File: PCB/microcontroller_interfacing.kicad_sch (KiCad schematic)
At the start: 19 parts, among them U3 CH340G, U4 USB_Micro_B, U5 AT24C256C-SSHL-T, X1 12MHz Crystal

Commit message: pcb revive
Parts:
- TP3: value TestPoint -> UsbOn
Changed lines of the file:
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@@
     (in_bom yes) (on_board yes)
     (property "Reference" "TP3" (id 0) (at 139.7 103.505 90))
-    (property "Value" "TestPoint" (id 1) (at 139.065 105.41 90))
+    (property "Value" "UsbOn" (id 1) (at 139.065 105.41 90))
     (property "Footprint" "TestPoint:TestPoint_Pad_D1.0mm" (id 2) (at 149.225 99.695 0)
       (effects (font (size 1.27 1.27)) hide)

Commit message: Add Justin's comments
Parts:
- removed R4: 2.7k, Resistor_SMD:R_0402_1005Metric, symbol Device:R
- removed R5: 4.7k, Resistor_SMD:R_0402_1005Metric, symbol Device:R
- added D?: DIODE, Footprint_EEE3088F:DO-214AC_L4.3-W2.7-LS5.3-RD, symbol Simulation_SPICE:DIODE
- R6: value 82 -> 150; footprint Resistor_SMD:R_0603_1608Metric -> Resistor_SMD:R_0402_1005Metric; JLC Part # C23255 -> C25082; Price 0.0015 -> 0.0007
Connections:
- net +5V: now also D?.2 (K); no longer C7.1, D4.2 (A), U3.4 (V3), U4.1 (VDD)
- net USB On: now also D4.1 (K), R6.1
- new net: C7.1, U3.4 (V3)
- new net USB_Detect: D4.2 (A), D?.1 (A), U4.1 (VDD)
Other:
- moved on the sheet: D4, R6

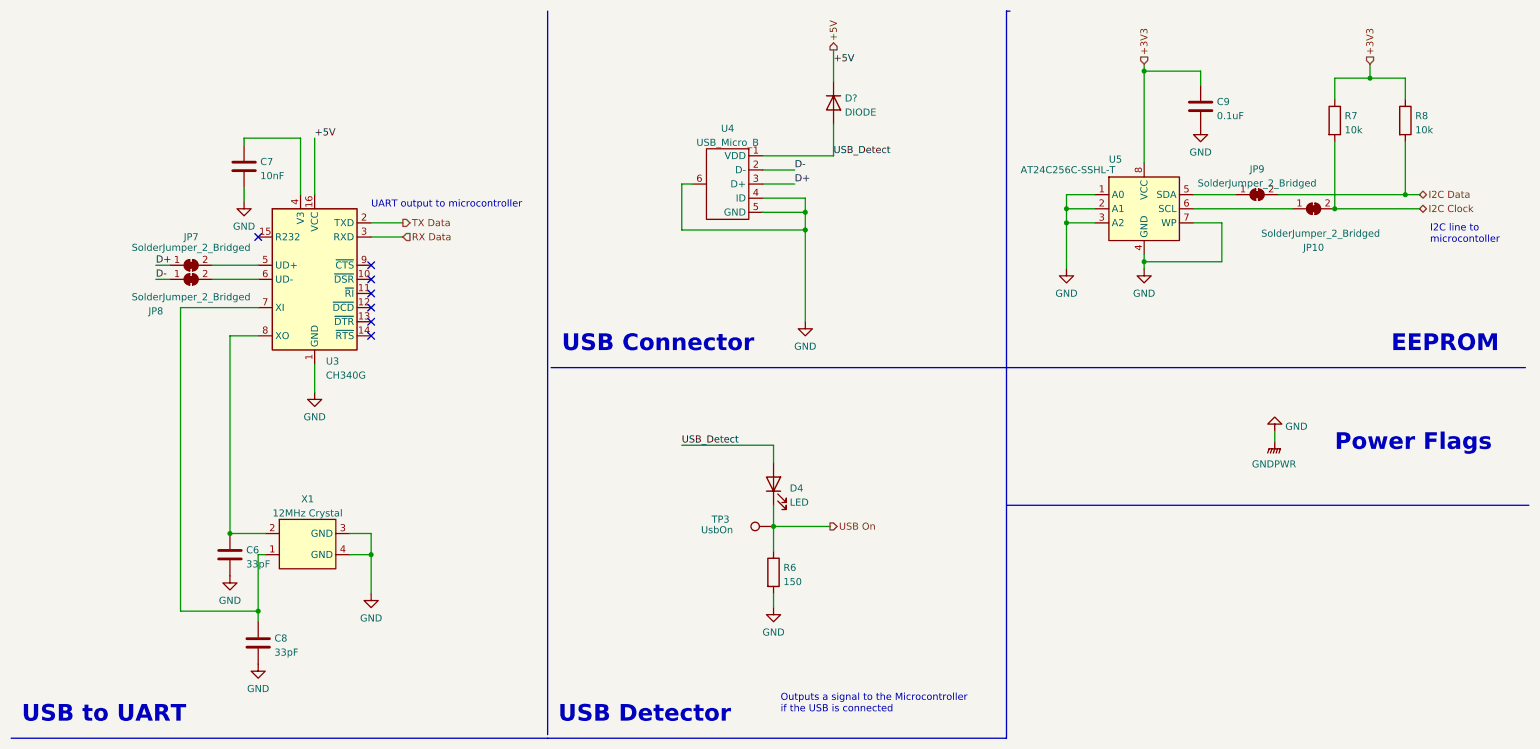
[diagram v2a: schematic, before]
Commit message: Mostly addressed issues with Sensing subsystem
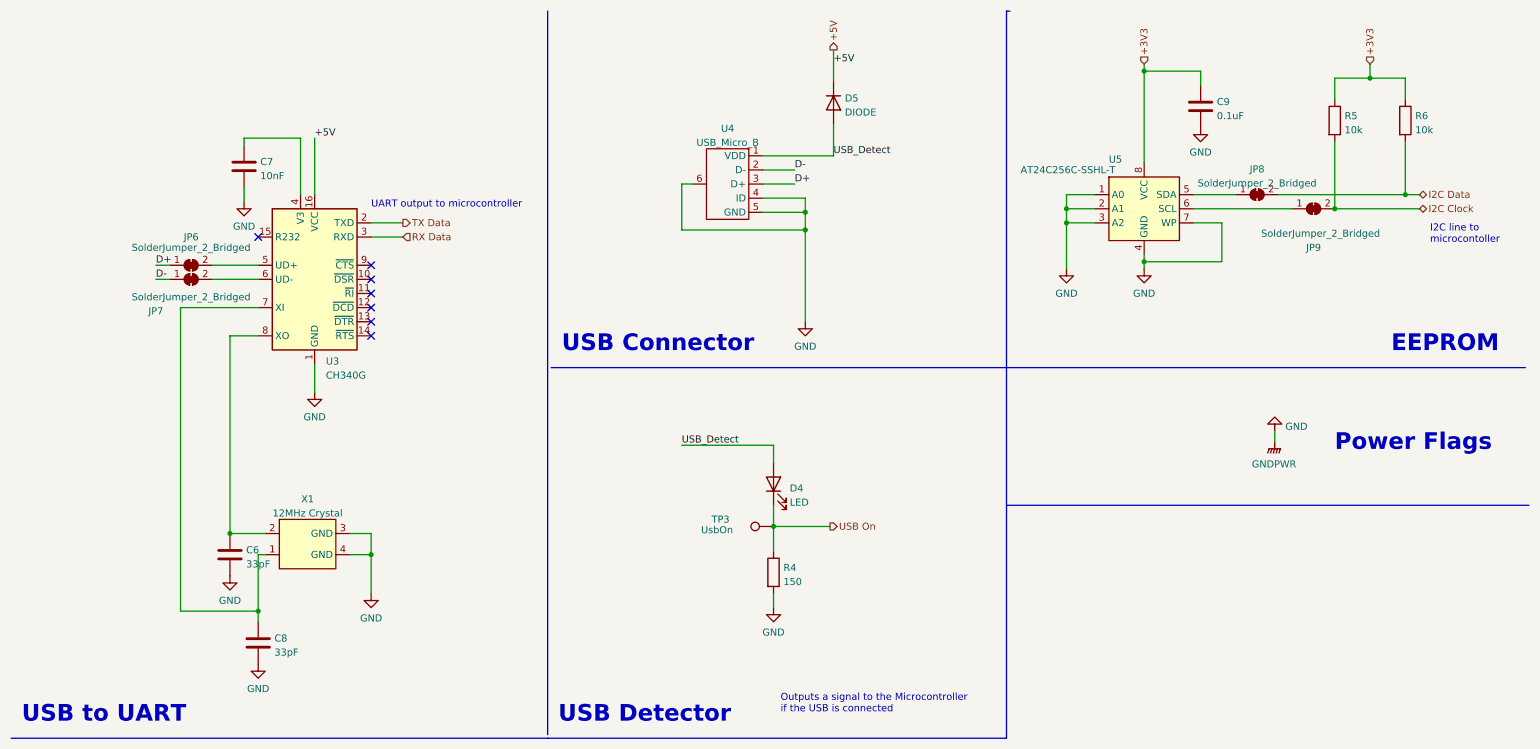
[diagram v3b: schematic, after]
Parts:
- gave numbers to parts that had none: 1
- renumbered JP7 to JP6, JP8 to JP7, JP9 to JP8, JP10 to JP9, R6 to R4, R7 to R5, R8 to R6
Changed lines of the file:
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@@
   (symbol (lib_id "power:GND") (at 215.9 58.42 0) (unit 1)
     (in_bom yes) (on_board yes) (fields_autoplaced)
-    (property "Reference" "#PWR030" (id 0) (at 215.9 64.77 0)
+    (property "Reference" "#PWR029" (id 0) (at 215.9 64.77 0)
       (effects (font (size 1.27 1.27)) hide)
     )
@@
   (symbol (lib_id "Jumper:SolderJumper_2_Bridged") (at 44.45 60.325 0) (unit 1)
     (in_bom yes) (on_board yes)
-    (property "Reference" "JP8" (id 0) (at 38.1 66.04 0))
+    (property "Reference" "JP7" (id 0) (at 38.1 66.04 0))
     (property "Value" "SolderJumper_2_Bridged" (id 1) (at 44.45 63.5 0))
     (property "Footprint" "Jumper:SolderJumper-2_P1.3mm_Bridged2Bar_Pad1.0x1.5mm" (id 2) (at 44.45 60.325 0)
@@
   (symbol (lib_id "power:GND") (at 226.06 33.02 0) (unit 1)
     (in_bom yes) (on_board yes) (fields_autoplaced)
-    (property "Reference" "#PWR031" (id 0) (at 226.06 39.37 0)
+    (property "Reference" "#PWR030" (id 0) (at 226.06 39.37 0)
       (effects (font (size 1.27 1.27)) hide)
     )
@@
   (symbol (lib_id "Jumper:SolderJumper_2_Bridged") (at 44.45 57.785 0) (unit 1)
     (in_bom yes) (on_board yes)
-    (property "Reference" "JP7" (id 0) (at 44.45 52.705 0))
+    (property "Reference" "JP6" (id 0) (at 44.45 52.705 0))
     (property "Value" "SolderJumper_2_Bridged" (id 1) (at 44.45 54.61 0))
     (property "Footprint" "Jumper:SolderJumper-2_P1.3mm_Bridged2Bar_Pad1.0x1.5mm" (id 2) (at 44.45 57.785 0)
@@
   (symbol (lib_id "Device:R") (at 262.89 31.75 0) (unit 1)
     (in_bom yes) (on_board yes) (fields_autoplaced)
-    (property "Reference" "R8" (id 0) (at 264.668 30.9153 0)
+    (property "Reference" "R6" (id 0) (at 264.668 30.9153 0)
       (effects (font (size 1.27 1.27)) (justify left))
     )
@@
   (symbol (lib_id "Device:R") (at 250.19 31.75 0) (unit 1)
     (in_bom yes) (on_board yes) (fields_autoplaced)
-    (property "Reference" "R7" (id 0) (at 251.968 30.9153 0)
+    (property "Reference" "R5" (id 0) (at 251.968 30.9153 0)
       (effects (font (size 1.27 1.27)) (justify left))
     )
@@
   (symbol (lib_id "Device:R") (at 149.225 113.03 0) (unit 1)
     (in_bom yes) (on_board yes) (fields_autoplaced)
-    (property "Reference" "R6" (id 0) (at 151.003 112.1953 0)
+    (property "Reference" "R4" (id 0) (at 151.003 112.1953 0)
       (effects (font (size 1.27 1.27)) (justify left))
     )
@@
   (symbol (lib_id "power:GNDPWR") (at 239.395 89.535 0) (unit 1)
     (in_bom yes) (on_board yes) (fields_autoplaced)
-    (property "Reference" "#PWR033" (id 0) (at 239.395 94.615 0)
+    (property "Reference" "#PWR032" (id 0) (at 239.395 94.615 0)
       (effects (font (size 1.27 1.27)) hide)
     )
@@
   (symbol (lib_id "power:GND") (at 239.395 87.63 180) (unit 1)
     (in_bom yes) (on_board yes) (fields_autoplaced)
-    (property "Reference" "#PWR032" (id 0) (at 239.395 81.28 0)
+    (property "Reference" "#PWR031" (id 0) (at 239.395 81.28 0)
       (effects (font (size 1.27 1.27)) hide)
     )
@@
   (symbol (lib_id "Simulation_SPICE:DIODE") (at 160.02 28.575 90) (unit 1)
     (in_bom yes) (on_board yes) (fields_autoplaced)
-    (property "Reference" "D?" (id 0) (at 162.052 27.7403 90)
+    (property "Reference" "D5" (id 0) (at 162.052 27.7403 90)
       (effects (font (size 1.27 1.27)) (justify right))
     )
@@
   (symbol (lib_id "Jumper:SolderJumper_2_Bridged") (at 246.38 47.625 0) (unit 1)
     (in_bom yes) (on_board yes)
-    (property "Reference" "JP10" (id 0) (at 246.38 54.61 0))
+    (property "Reference" "JP9" (id 0) (at 246.38 54.61 0))
     (property "Value" "SolderJumper_2_Bridged" (id 1) (at 247.65 52.07 0))
     (property "Footprint" "Jumper:SolderJumper-2_P1.3mm_Bridged2Bar_Pad1.0x1.5mm" (id 2) (at 246.38 47.625 0)
@@
   (symbol (lib_id "Jumper:SolderJumper_2_Bridged") (at 236.22 45.085 0) (unit 1)
     (in_bom yes) (on_board yes) (fields_autoplaced)
-    (property "Reference" "JP9" (id 0) (at 236.22 40.4962 0))
+    (property "Reference" "JP8" (id 0) (at 236.22 40.4962 0))
     (property "Value" "SolderJumper_2_Bridged" (id 1) (at 236.22 43.0331 0))
     (property "Footprint" "Jumper:SolderJumper-2_P1.3mm_Bridged2Bar_Pad1.0x1.5mm" (id 2) (at 236.22 45.085 0)
@@
   (symbol (lib_id "power:GND") (at 201.93 58.42 0) (unit 1)
     (in_bom yes) (on_board yes) (fields_autoplaced)
-    (property "Reference" "#PWR029" (id 0) (at 201.93 64.77 0)
-      (effects (font (size 1.27 1.27)) hide)
-    )
+    (property "Reference" "#PWR028" (id 0) (at 201.93 64.77 0)
+      (effects (font (size 1.27 1.27)) hide)
+    )

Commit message: Prepare PCB
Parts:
- C6, C8: LCSC (none) -> C1562
- C7: LCSC (none) -> C15195
- C9: value 0.1uF -> 100nF; LCSC (none) -> C1525; Price 0.0011 -> (none)
- D4: value LED -> RLED; LCSC (none) -> C2286
- D5: LCSC (none) -> C95872
- R4: LCSC (none) -> C25082
- R5, R6: LCSC (none) -> C25744
- U3: LCSC (none) -> C14267
- U4: LCSC (none) -> C404969
- U5: LCSC (none) -> C6482
- X1: LCSC (none) -> C9002
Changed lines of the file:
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@@
+      (effects (font (size 1.27 1.27)) hide)
+    )
+    (property "LCSC" "C1562" (id 7) (at 51.435 109.855 0)
       (effects (font (size 1.27 1.27)) hide)
     )
@@
       (effects (font (size 1.27 1.27)) hide)
     )
+    (property "LCSC" "C404969" (id 8) (at 139.7 43.18 0)
+      (effects (font (size 1.27 1.27)) hide)
+    )
     (pin "1")
     (pin "2")
@@
       (effects (font (size 1.27 1.27)) (justify left))
     )
-    (property "Value" "0.1uF" (id 1) (at 228.981 30.9122 0)
+    (property "Value" "100nF" (id 1) (at 228.981 30.9122 0)
       (effects (font (size 1.27 1.27)) (justify left))
     )
@@
       (effects (font (size 1.27 1.27)) hide)
     )
-    (property "Price" "0.0011" (id 5) (at 226.06 29.21 0)
+    (property "Price" "" (id 5) (at 226.06 29.21 0)
       (effects (font (size 1.27 1.27)) hide)
     )
     (property "Extended/Basic" "B" (id 6) (at 226.06 29.21 0)
+      (effects (font (size 1.27 1.27)) hide)
+    )
+    (property "LCSC" "C1525" (id 7) (at 226.06 29.21 0)
       (effects (font (size 1.27 1.27)) hide)
     )
@@
     )
     (property "Extended/Basic" "B" (id 7) (at 215.9 47.625 0)
+      (effects (font (size 1.27 1.27)) hide)
+    )
+    (property "LCSC" "C6482" (id 8) (at 215.9 47.625 0)
       (effects (font (size 1.27 1.27)) hide)
     )
@@
       (effects (font (size 1.27 1.27)) hide)
     )
+    (property "LCSC" "C9002" (id 8) (at 65.405 107.315 0)
+      (effects (font (size 1.27 1.27)) hide)
+    )
     (pin "1")
     (pin "2")
@@
       (effects (font (size 1.27 1.27)) hide)
     )
+    (property "LCSC" "C25744" (id 7) (at 262.89 31.75 0)
+      (effects (font (size 1.27 1.27)) hide)
+    )
     (pin "1")
     (pin "2")
@@
     )
     (property "Extended/Basic" "B" (id 6) (at 250.19 31.75 0)
+      (effects (font (size 1.27 1.27)) hide)
+    )
+    (property "LCSC" "C25744" (id 7) (at 250.19 31.75 0)
       (effects (font (size 1.27 1.27)) hide)
     )
@@
       (effects (font (size 1.27 1.27)) hide)
     )
+    (property "LCSC" "C15195" (id 7) (at 53.975 40.005 0)
+      (effects (font (size 1.27 1.27)) hide)
+    )
     (pin "1")
     (pin "2")
@@
       (effects (font (size 1.27 1.27)) hide)
     )
+    (property "LCSC" "C25082" (id 7) (at 149.225 113.03 0)
+      (effects (font (size 1.27 1.27)) hide)
+    )
     (pin "1")
     (pin "2")
@@
       (effects (font (size 1.27 1.27)) hide)
     )
+    (property "LCSC" "C95872" (id 8) (at 160.02 28.575 0)
+      (effects (font (size 1.27 1.27)) hide)
+    )
     (pin "1")
     (pin "2")
@@
     )
     (property "Extended/Basic" "B" (id 6) (at 56.515 125.73 0)
+      (effects (font (size 1.27 1.27)) hide)
+    )
+    (property "LCSC" "C1562" (id 7) (at 56.515 125.73 0)
       (effects (font (size 1.27 1.27)) hide)
     )
@@
     )
     (property "Extended/Basic" "E" (id 7) (at 66.675 60.325 0)
+      (effects (font (size 1.27 1.27)) hide)
+    )
+    (property "LCSC" "C14267" (id 8) (at 66.675 60.325 0)
       (effects (font (size 1.27 1.27)) hide)
     )
@@
       (effects (font (size 1.27 1.27)) (justify right))
     )
-    (property "Value" "LED" (id 1) (at 152.146 100.4447 90)
+    (property "Value" "RLED" (id 1) (at 152.146 100.4447 90)
       (effects (font (size 1.27 1.27)) (justify right))
     )
@@
       (effects (font (size 1.27 1.27)) hide)
     )
+    (property "LCSC" "C2286" (id 7) (at 149.225 97.155 0)
+      (effects (font (size 1.27 1.27)) hide)
+    )
